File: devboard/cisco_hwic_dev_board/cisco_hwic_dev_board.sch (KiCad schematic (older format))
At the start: 19 parts, among them J1 Conn_02x20_Odd_Even, J2 Conn_02x34_Top_Bottom_Cisco, J3 Conn_01x15, J4 USB Blaster Active Serial, J5 ATT85_VIN, J6 SD Card, J7 Power, U1 AT25xxx, U2 ATtiny85_devboard

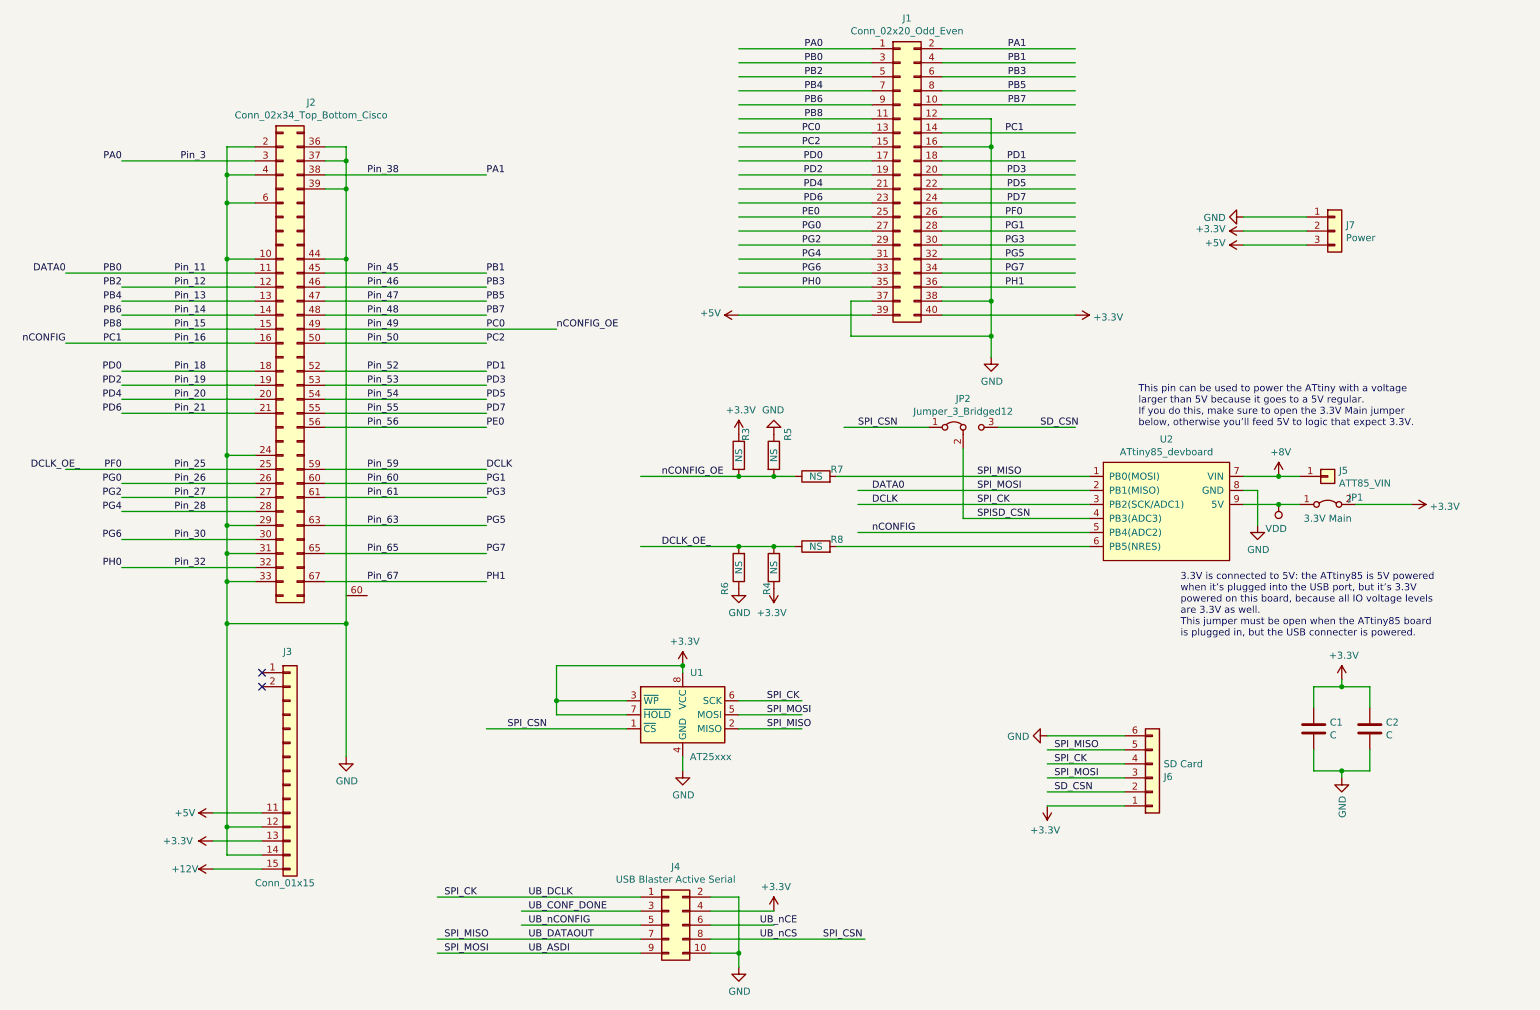
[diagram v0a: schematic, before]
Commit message: Remove 2 resistors. Connect AT_PB5.
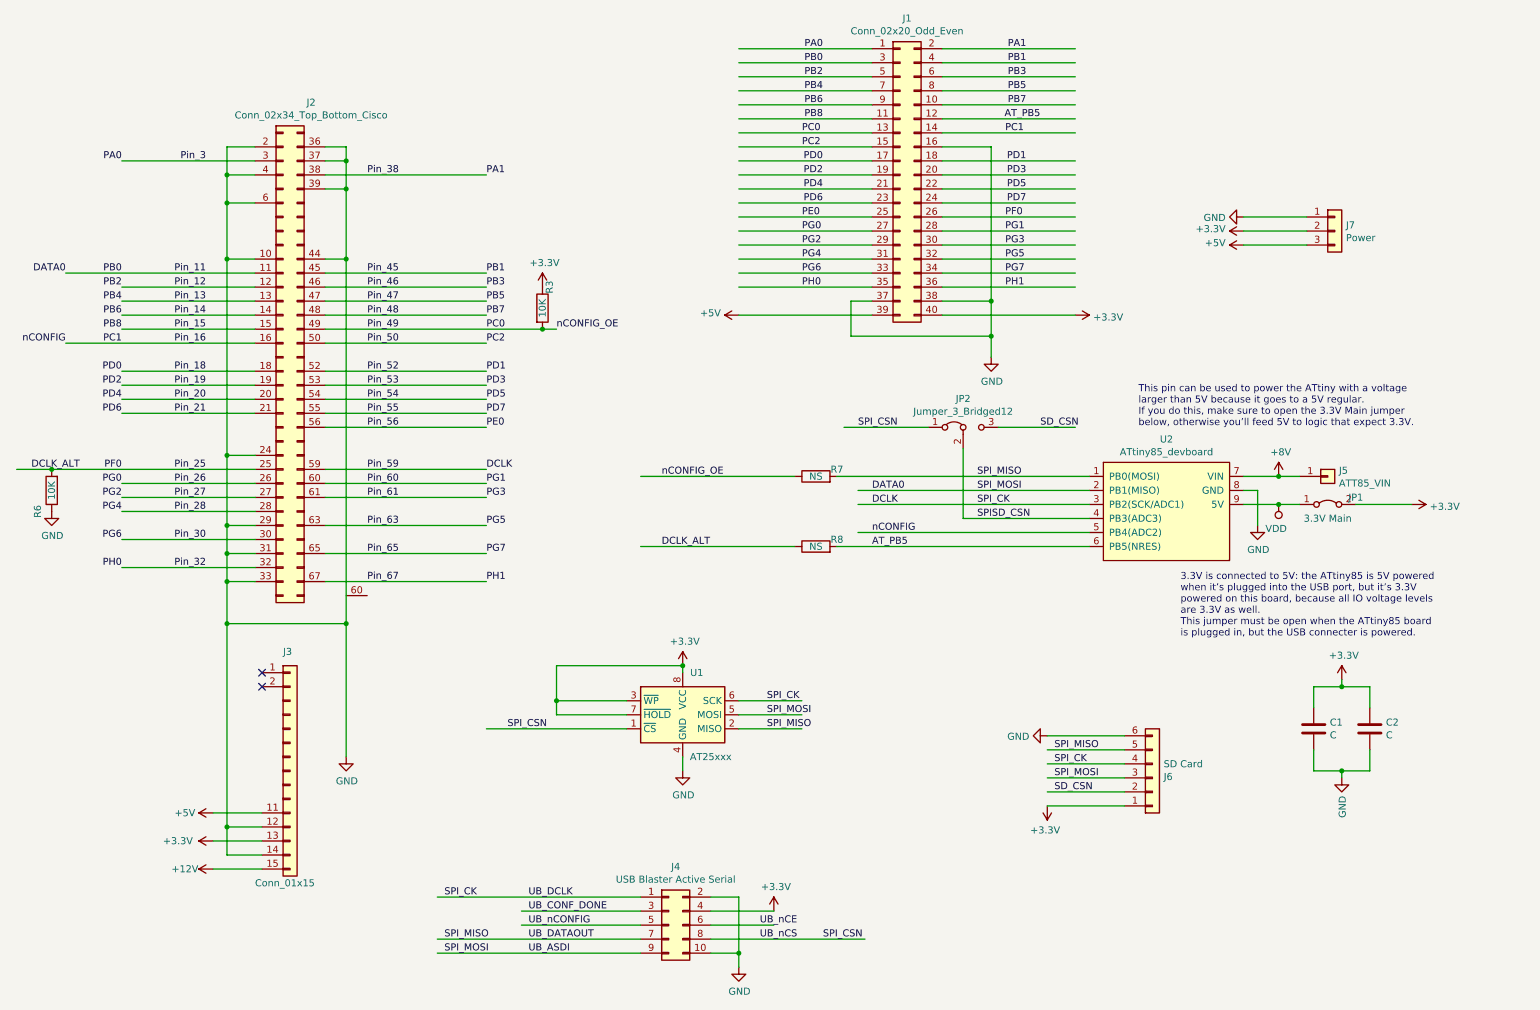
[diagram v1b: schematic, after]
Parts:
- removed R4, R5: NS, Resistor_SMD:R_0603_1608Metric_Pad1.05x0.95mm_HandSolder, symbol Device:R
- R3, R6: value NS -> 10K
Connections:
- net labels added: AT_PB5, DCLK_ALT
- net labels removed: DCLK_OE_
- wire segments 178 -> 175
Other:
- moved on the sheet: R3, R6
